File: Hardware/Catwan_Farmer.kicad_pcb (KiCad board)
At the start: 2 copper layers, 60 x 70 mm, 56 parts, among them J1 SENSOR 1, J10 VSP, J2 SENSOR 2, J3 SENSOR 3, J4 BATT, J5 USB_B, J6 Conn_01x04, J7 DHT22, J9 SENSOR 4, SW1 SW_Push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

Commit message: New size pcb
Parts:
- removed REF** (x4): MountingHole_3.2mm_M3_Pad_Via, MountingHole:MountingHole_3.2mm_M3_Pad_Via
- J6: moved to B.Cu
- moved SW1 30.1 mm to (120.9, 100.8)
- moved R5 17.1 mm to (136.8, 64.0), turned to 180 degrees
- moved J4 16.2 mm to (120.3, 77.9)
- moved J10 16.2 mm to (120.3, 69.9)
- moved AE1 15.4 mm to (145.3, 59.2)
- moved D7 14.8 mm to (136.8, 62.0), turned to 0 degrees
- moved U1 13.5 mm to (136.1, 71.5)
- moved D1 13.0 mm to (129.8, 68.3)
- moved D2 13.0 mm to (129.8, 72.9)
- moved D3 13.0 mm to (129.8, 70.6)
- moved D10 12.8 mm to (136.8, 60.1), turned to 0 degrees
- moved R7 12.0 mm to (144.8, 89.5)
- moved R4 12.0 mm to (144.8, 87.6)
- moved J7 11.1 mm to (161.0, 106.1)
- moved U4 11.0 mm to (130.5, 58.1)
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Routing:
- net +3V3: track 187.7 -> 0.00 mm, vias 5 -> 0
- net /BAT: track 90.4 -> 0.00 mm, vias 2 -> 0
- net GND: track 71.6 -> 1.27 mm, vias 18 -> 0
- net /EN: track 52.3 -> 0.00 mm, vias 2 -> 0
- net /SENS_Y: track 50.6 -> 0.00 mm, vias 3 -> 0
- net /SENS_X: track 47.3 -> 0.00 mm, vias 2 -> 0
- net Net-(D5-Pad2): track 43.4 -> 0.00 mm, vias 2 -> 0
- net /D-: track 43.3 -> 0.00 mm
- net VCC: track 43.2 -> 0.00 mm, vias 2 -> 0
- net /DIO1: track 42.9 -> 0.00 mm, vias 2 -> 0
- net Net-(D5-Pad1): track 41.7 -> 0.00 mm, vias 2 -> 0
- net /D+: track 41.6 -> 0.00 mm
- net /DHT_DAT: track 41.3 -> 0.00 mm, vias 2 -> 0
- net /DIO2: track 40.7 -> 0.00 mm, vias 2 -> 0
- net /DIO0: track 39.3 -> 0.00 mm, vias 2 -> 0
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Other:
- board size 60 x 70 mm -> 51.8 x 53.6 mm

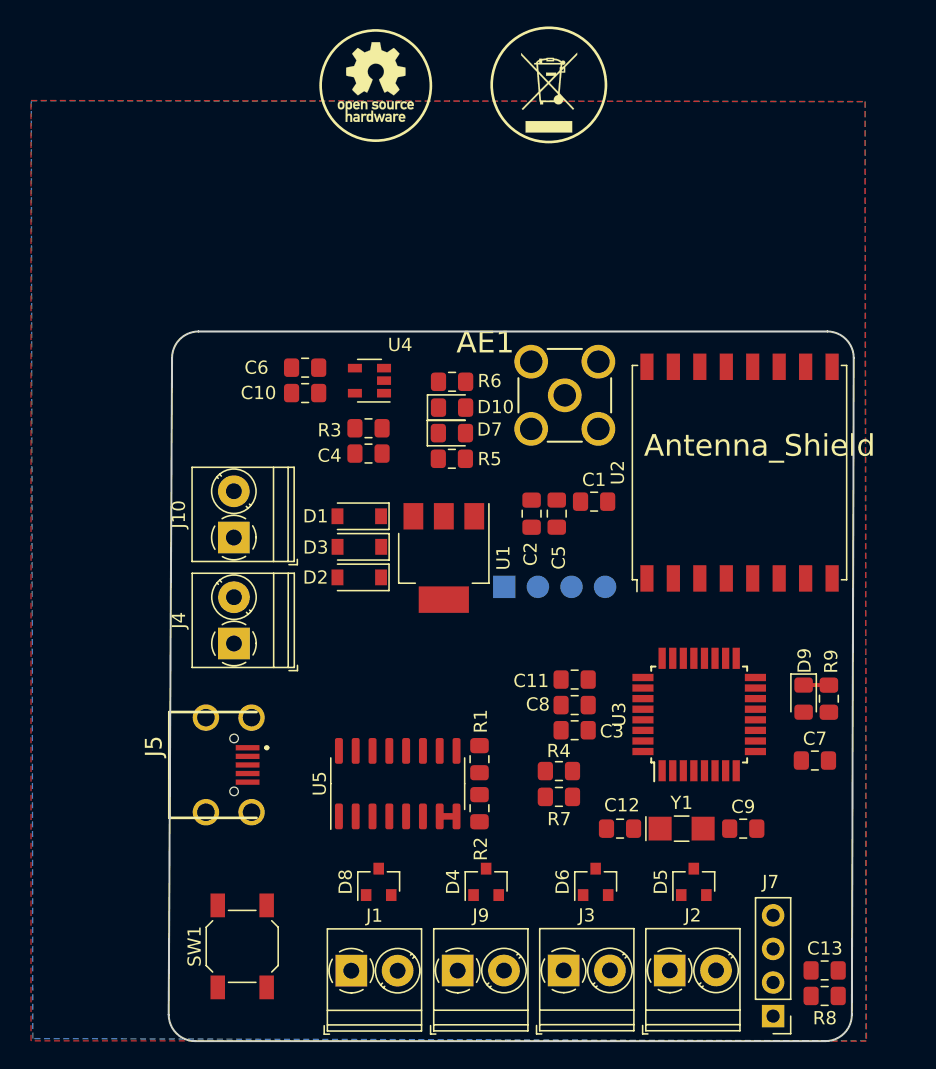
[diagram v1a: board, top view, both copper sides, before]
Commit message: Routeo new size pcb
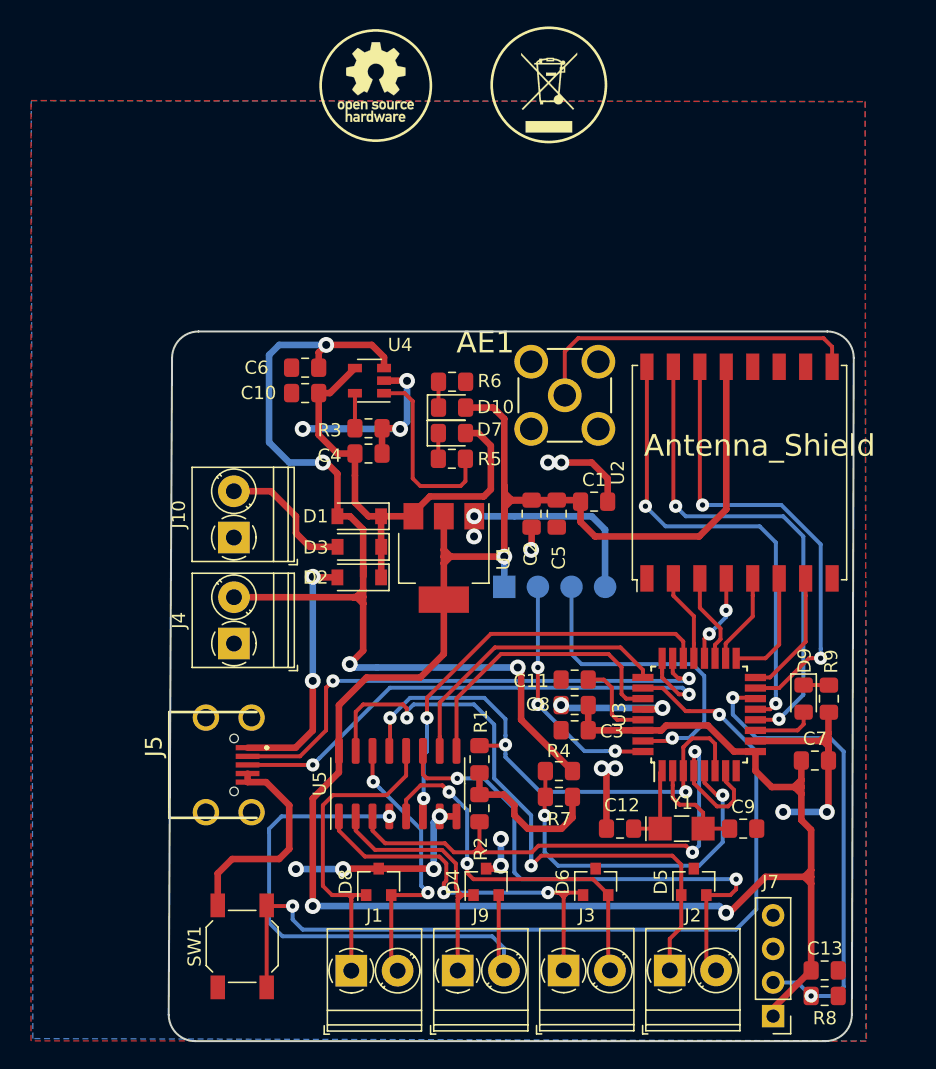
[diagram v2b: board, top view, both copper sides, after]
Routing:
- net +3V3: track 0.00 -> 175.9 mm, vias 0 -> 3
- net GND: track 1.27 -> 126.7 mm, vias 0 -> 20
- net /BAT: track 0.00 -> 75.9 mm, vias 0 -> 4
- net Net-(SW1-Pad2): track 0.00 -> 68.0 mm, vias 0 -> 2
- net Net-(D5-Pad1): track 0.00 -> 51.0 mm, vias 0 -> 2
- net /SENS_Y: track 0.00 -> 46.7 mm, vias 0 -> 2
- net Net-(D4-Pad2): track 0.00 -> 42.7 mm, vias 0 -> 1
- net /D+: track 0.00 -> 41.1 mm, vias 0 -> 2
- net Net-(D5-Pad2): track 0.00 -> 40.7 mm, vias 0 -> 2
- net /SENS_X: track 0.00 -> 40.5 mm, vias 0 -> 3
- net /D-: track 0.00 -> 40.2 mm, vias 0 -> 2
- net /DIO1: track 0.00 -> 37.6 mm, vias 0 -> 2
- net /DHT_DAT: track 0.00 -> 36.4 mm, vias 0 -> 2
- net VCC: track 0.00 -> 35.6 mm
- net /DIO2: track 0.00 -> 35.5 mm, vias 0 -> 2
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
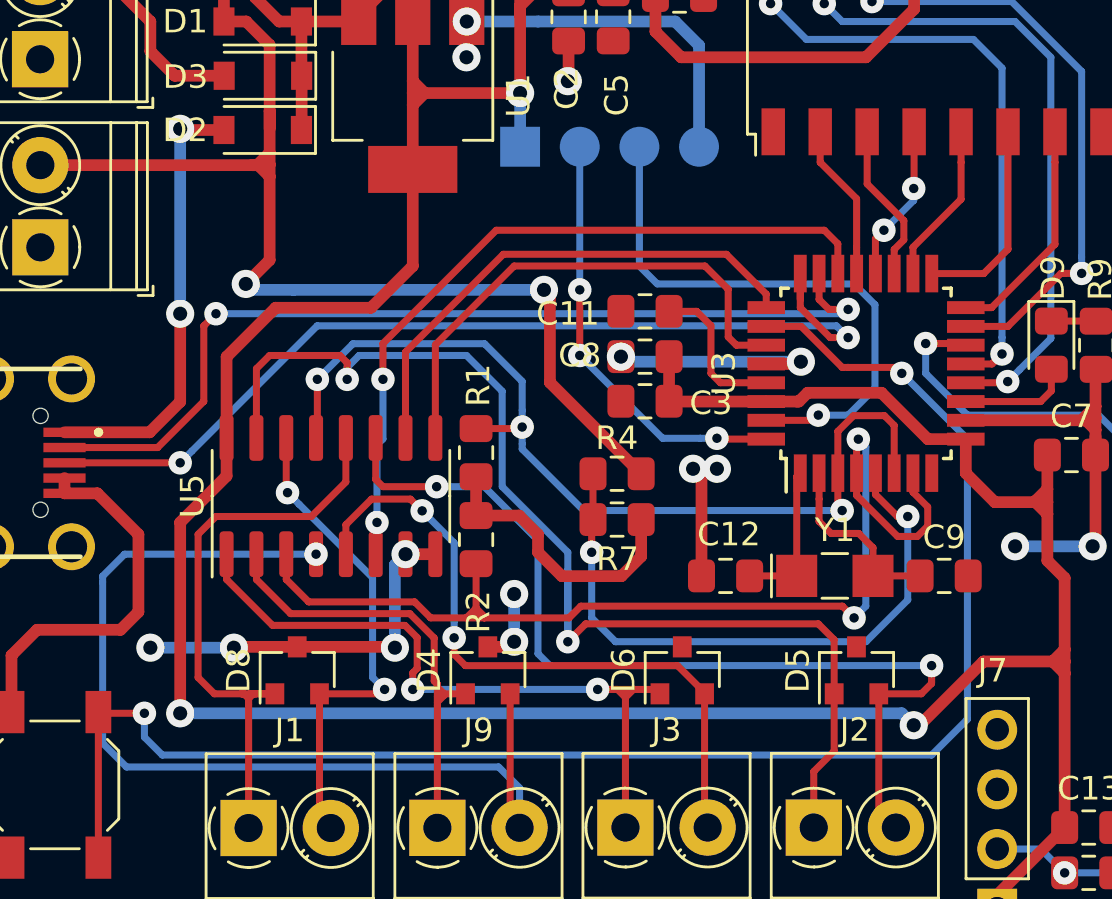
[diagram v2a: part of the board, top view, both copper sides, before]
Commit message: Fix tracks samd
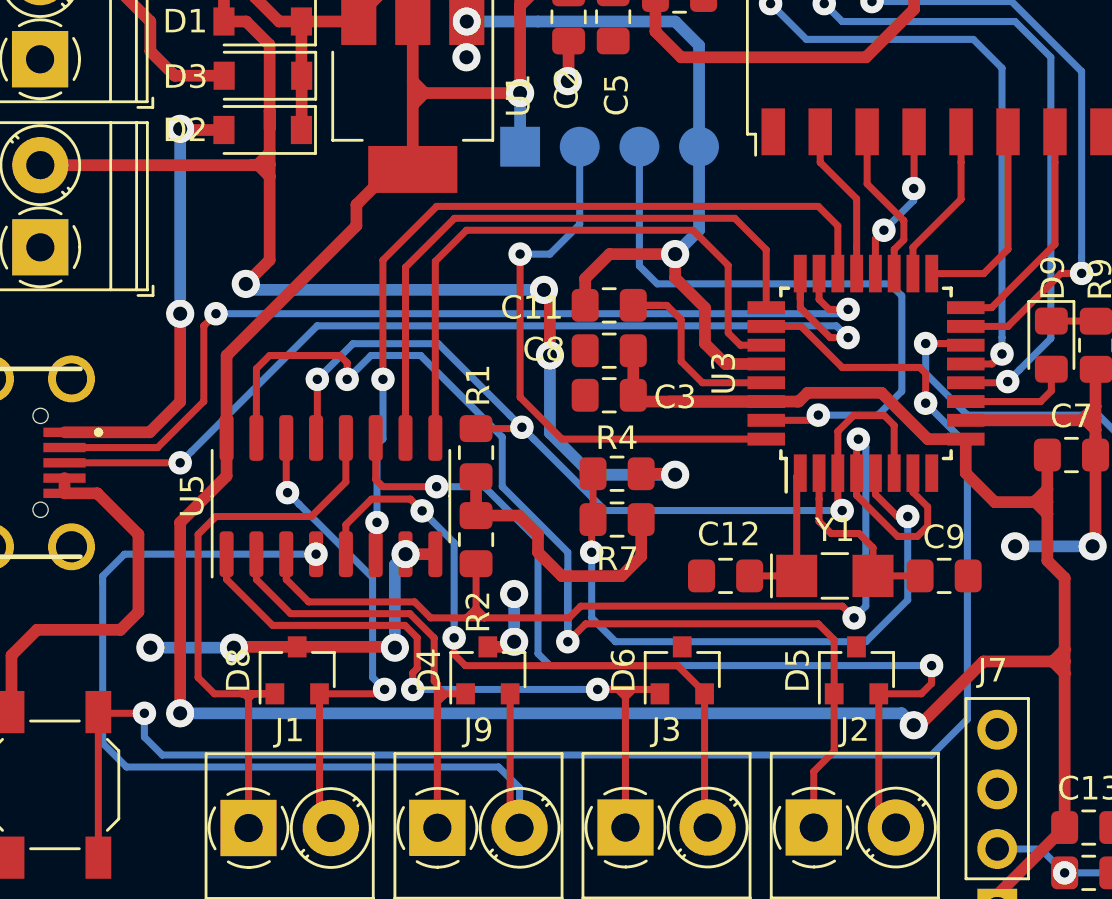
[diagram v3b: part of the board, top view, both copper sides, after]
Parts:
- moved C11 1.55 mm to (144.5, 80.4)
- moved C3 1.55 mm to (144.5, 84.2)
- moved C8 1.55 mm to (144.5, 82.3)
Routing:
- net /SWDIO: track 18.3 -> 23.7 mm, vias 3 -> 1
- net /S0: track 22.0 -> 26.5 mm
- net /BAT: track 75.9 -> 80.1 mm, vias 4 -> 6
- net +3V3: track 175.9 -> 179.8 mm
- net /S1: track 22.0 -> 25.9 mm
- net /EN: track 32.0 -> 35.4 mm
- net GND: track 126.7 -> 129.4 mm, vias 20 -> 17
- net Net-(C11-Pad2): track 6.59 -> 9.24 mm
- net /SWCLK: track 24.5 -> 27.1 mm
- net /SENS_X: track 40.5 -> 38.8 mm
- net Net-(D5-Pad1): track 51.0 -> 49.6 mm

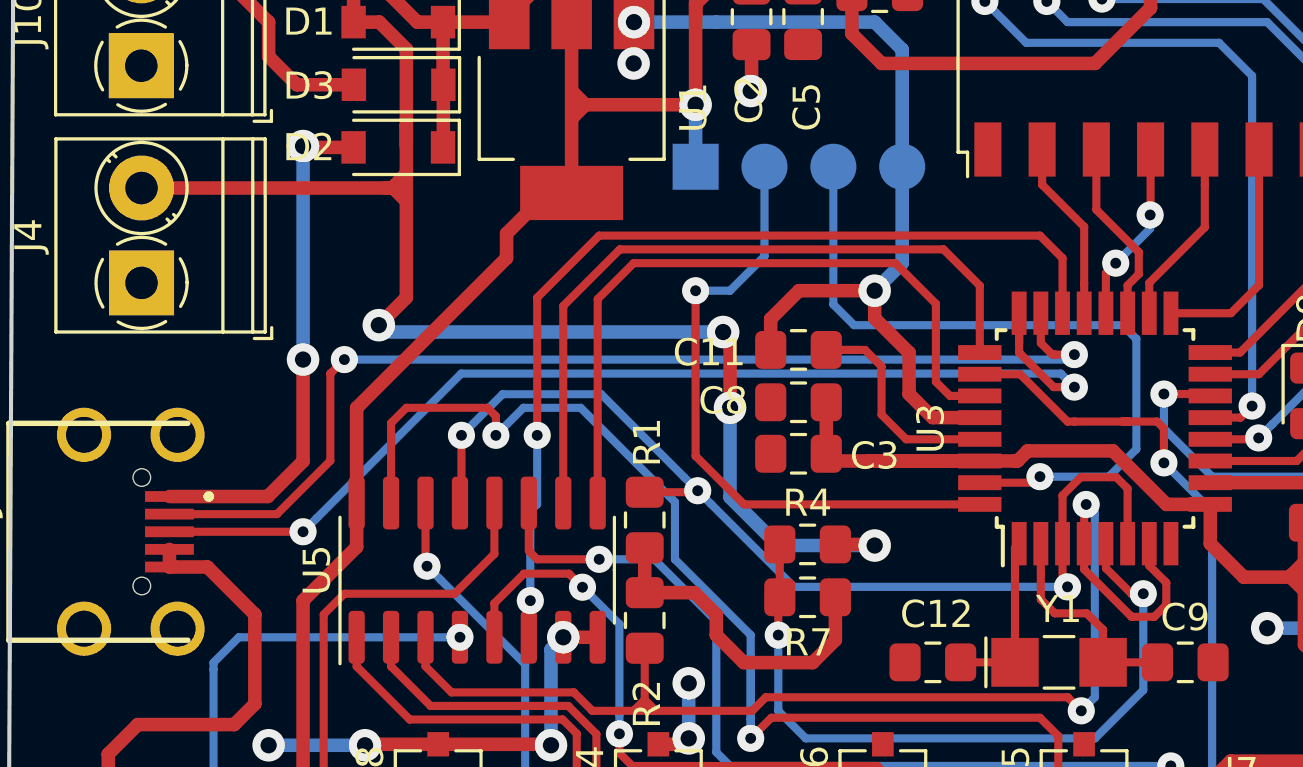
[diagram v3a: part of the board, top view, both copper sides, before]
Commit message: Change tracks D- D+
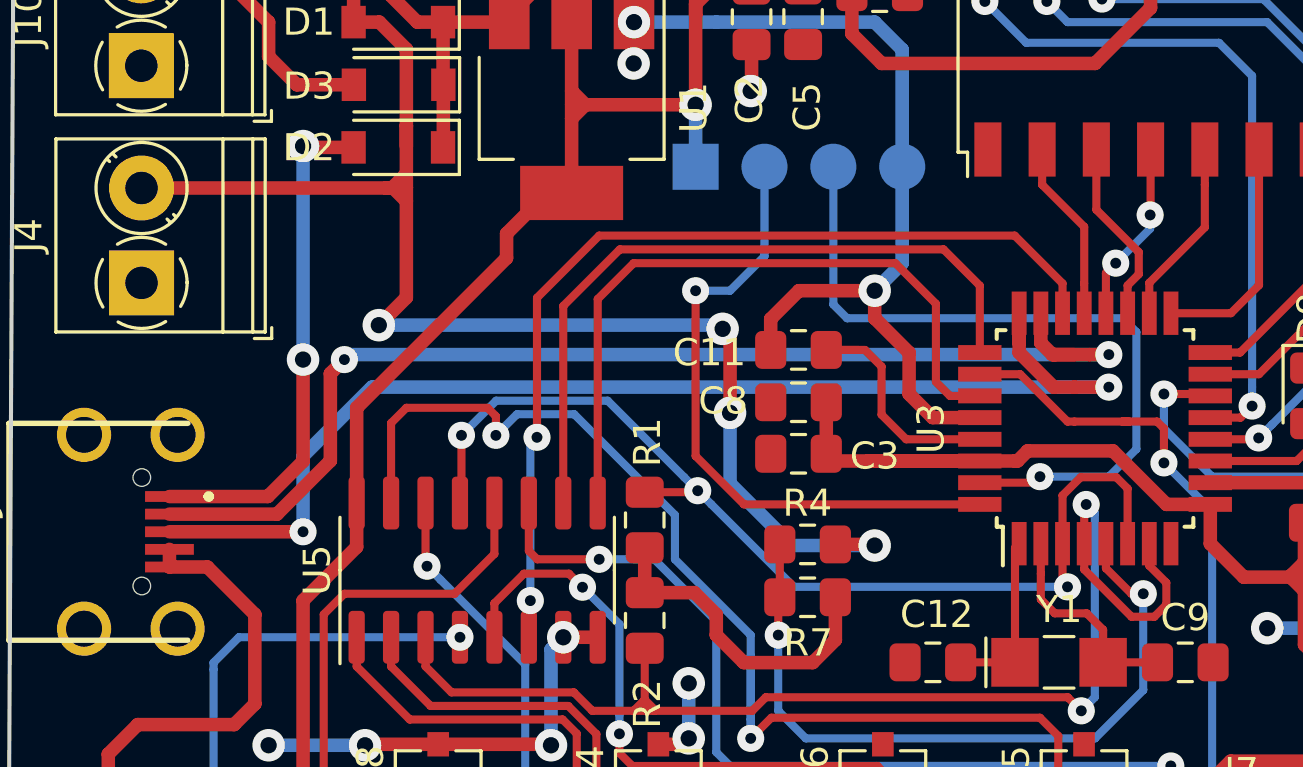
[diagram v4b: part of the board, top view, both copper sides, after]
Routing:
- net /D+: track 41.1 -> 44.9 mm
- net /D-: track 40.2 -> 43.6 mm
- net /EN: track 35.4 -> 34.8 mm

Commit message: Update V1.0
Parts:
- removed the REF*** at (144.1, 36.3)
- removed the REF*** at (131.0, 35.5)
- added G***: LOGO, Aesthetics:electronic_cats_logo_8x6, B.Cu at (125.4, 60.2)
- added G***: LOGO, Aesthetics:electronic_cats_logo_4x3, F.Cu at (126.7, 87.7)
- added svg2mod: electronic, Aesthetics:titule_electronic_med, B.Cu at (143.9, 82.2)
- D10: value LED -> ON
- J6: value Conn_01x04 -> SWD
- SW1: value SW_Push -> RST
- moved REF*** 47.8 mm to (154.4, 62.2)
- moved R2 24.3 mm to (162.7, 94.8), turned to 270 degrees
- moved R1 23.4 mm to (160.8, 94.8)
- moved R7 19.7 mm to (128.1, 79.1)
- moved R4 19.7 mm to (128.1, 77.2)
- moved J1 19.4 mm to (148.4, 104.3), turned to 180 degrees
- moved D6 17.2 mm to (130.4, 97.4), turned to 270 degrees
- moved D8 15.5 mm to (146.7, 97.5), turned to 270 degrees
- moved C5 15.3 mm to (132.3, 77.2), turned to 180 degrees
- moved C2 15.1 mm to (132.4, 79.1), turned to 180 degrees
- moved J3 13.1 mm to (132.2, 104.3), turned to 180 degrees
- moved C4 8.82 mm to (138.2, 67.7), turned to 180 degrees
- moved C9 4.34 mm to (154.4, 92.1), turned to 270 degrees
- moved C3 4.31 mm to (148.5, 85.8), turned to 270 degrees
- moved C8 4.04 mm to (146.6, 85.8), turned to 270 degrees
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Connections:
- J3 pad 1: Net-(D6-Pad1) -> Net-(D6-Pad2)
- J3 pad 2: Net-(D6-Pad2) -> Net-(D6-Pad1)
- J6 pad 2: /SWDIO -> /SWCLK
- J6 pad 3: /SWCLK -> /SWDIO
- U5 pad 1: Net-(D6-Pad1) -> Net-(D6-Pad2)
- U5 pad 5: Net-(D6-Pad2) -> Net-(D6-Pad1)
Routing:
- net +3V3: track 179.8 -> 112.7 mm
- net /ADC_BAT: track 27.0 -> 81.6 mm
- net /SENS_Y: track 46.7 -> 79.6 mm, vias 2 -> 3
- net /EN: track 34.8 -> 61.1 mm
- net Net-(D4-Pad2): track 42.7 -> 21.2 mm, vias 1 -> 0
- net /SS: track 6.89 -> 28.3 mm, vias 0 -> 2
- net Net-(AE1-Pad1): track 25.7 -> 6.09 mm
- net /DIO5: track 9.71 -> 27.2 mm, vias 0 -> 2
- net /BAT: track 79.8 -> 63.3 mm, vias 6 -> 2
- net /DIO2: track 35.5 -> 22.2 mm
- net /SCK: track 6.72 -> 20.0 mm, vias 2 -> 0
- net Net-(D5-Pad1): track 49.1 -> 36.0 mm, vias 2 -> 0
- net /RFM_RST: track 8.68 -> 21.4 mm, vias 0 -> 2
- net Net-(D5-Pad2): track 40.7 -> 29.3 mm, vias 2 -> 0
- net /DIO1: track 37.6 -> 26.6 mm
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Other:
- board text added: "+"
- board text added: "-"
- board text added: "3V3"
- board text added: "BATT"
- board text added: "CLK"
- board text added: "CatWAN Farmer"
- board text added: "DIO"
- board text added: "GND"
- board text added: "S1"
- board text added: "S2"
- board text added: "S3"
- board text added: "S4"
- board text added: "VSP"
- board text added: "v1.0"
